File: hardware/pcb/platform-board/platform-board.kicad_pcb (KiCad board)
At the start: 2 copper layers, 55 x 65 mm, 9 parts, among them J1 Conn_01x09_Pin, J2 Conn_01x05_Pin, J3 Conn_01x05_Pin, J4 Conn_01x05_Pin, J5 Conn_01x05_Pin

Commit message: Initial boards for raw prototyping
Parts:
- J1: footprint Connector_PinHeader_2.54mm:PinHeader_1x09_P2.54mm_Horizontal -> TwinOak platform footprints:82155700
- moved J1 26.1 mm to (144.5, 91.7), turned to 0 degrees
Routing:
- net GND: track 71.1 -> 91.2 mm, vias 0 -> 1
- net Net-(J1-Pin_5): track 73.7 -> 53.8 mm, vias 2 -> 1
- net Net-(J1-Pin_6): track 73.7 -> 55.6 mm, vias 2 -> 1
- net Net-(J1-Pin_4): track 71.1 -> 53.8 mm, vias 2 -> 1
- net Net-(J1-Pin_7): track 71.1 -> 56.9 mm, vias 2 -> 1
- net Net-(J1-Pin_3): track 68.6 -> 55.0 mm, vias 2 -> 1
- net Net-(J1-Pin_8): track 68.6 -> 56.8 mm, vias 2 -> 1
- net Net-(J1-Pin_2): track 66.0 -> 54.4 mm, vias 2 -> 4
- net Net-(J1-Pin_9): track 66.0 -> 58.1 mm, vias 2 -> 1
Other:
- board text added: "Platform baseboard v1.0 TwinOak Standard Repeater"

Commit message: Platform rewire
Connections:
- J2 pad 2: Net-(J1-Pin_2) -> Net-(J1-Pin_3)
- J2 pad 3: Net-(J1-Pin_3) -> Net-(J1-Pin_5)
- J2 pad 4: Net-(J1-Pin_4) -> Net-(J1-Pin_7)
- J2 pad 5: Net-(J1-Pin_5) -> Net-(J1-Pin_9)
- J3 pad 2: Net-(J1-Pin_2) -> Net-(J1-Pin_3)
- J3 pad 3: Net-(J1-Pin_3) -> Net-(J1-Pin_5)
- J3 pad 4: Net-(J1-Pin_4) -> Net-(J1-Pin_7)
- J3 pad 5: Net-(J1-Pin_5) -> Net-(J1-Pin_9)
- J4 pad 2: Net-(J1-Pin_6) -> Net-(J1-Pin_2)
- J4 pad 3: Net-(J1-Pin_7) -> Net-(J1-Pin_4)
- J4 pad 4: Net-(J1-Pin_8) -> Net-(J1-Pin_6)
- J4 pad 5: Net-(J1-Pin_9) -> Net-(J1-Pin_8)
- J5 pad 2: Net-(J1-Pin_6) -> Net-(J1-Pin_2)
- J5 pad 3: Net-(J1-Pin_7) -> Net-(J1-Pin_4)
- J5 pad 4: Net-(J1-Pin_8) -> Net-(J1-Pin_6)
- J5 pad 5: Net-(J1-Pin_9) -> Net-(J1-Pin_8)
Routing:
- net Net-(J1-Pin_2): track 54.4 -> 62.0 mm, vias 4 -> 1
- net Net-(J1-Pin_4): track 53.8 -> 61.0 mm
- net Net-(J1-Pin_5): track 53.8 -> 58.9 mm
- net Net-(J1-Pin_6): track 55.6 -> 59.9 mm
- net Net-(J1-Pin_3): track 55.0 -> 58.8 mm, vias 1 -> 2
- net Net-(J1-Pin_7): track 56.9 -> 59.9 mm
- net Net-(J1-Pin_9): track 58.1 -> 61.0 mm
- net Net-(J1-Pin_8): track 56.8 -> 58.9 mm
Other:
- board text added: "Platform baseboard v1.1 TwinOak Standard Repeater"
- board text removed: "Platform baseboard v1.0 TwinOak Standard Repeater"

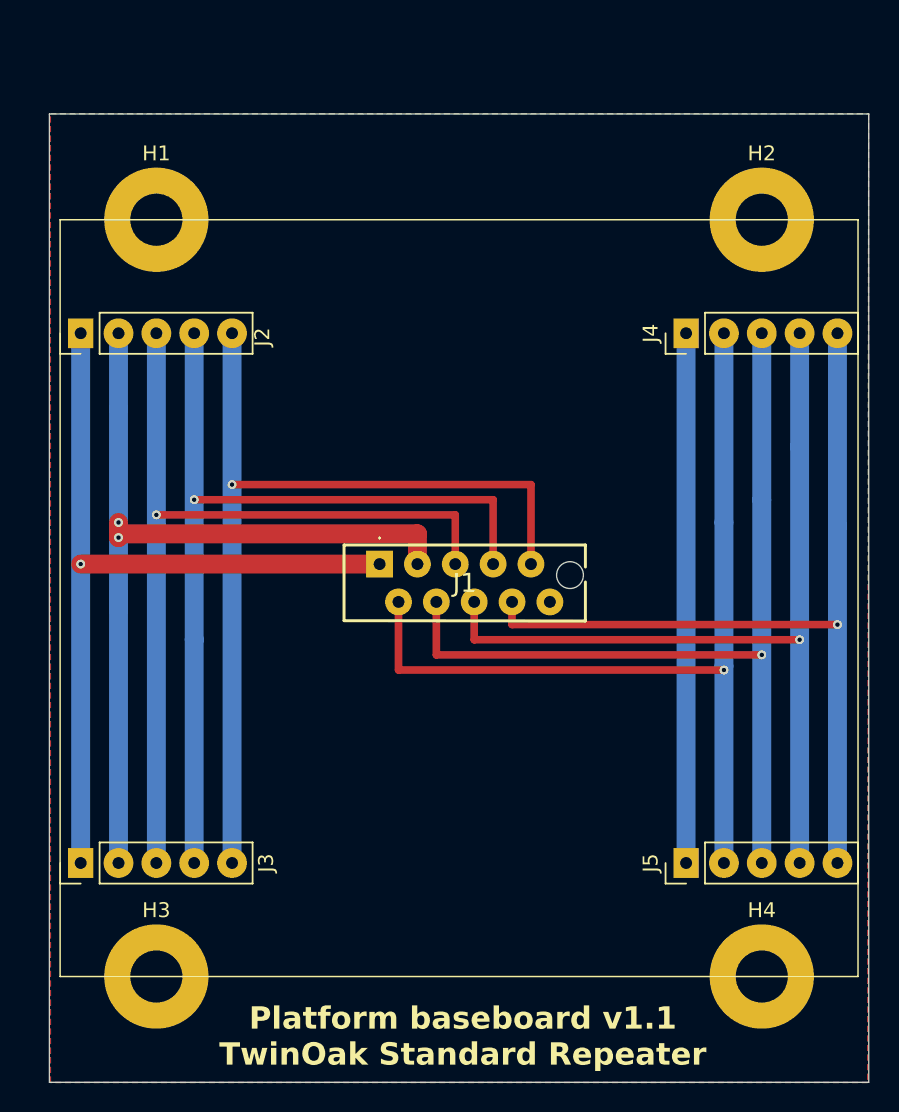
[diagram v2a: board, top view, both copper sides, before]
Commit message: Final PCB adjuments to rev 1.1
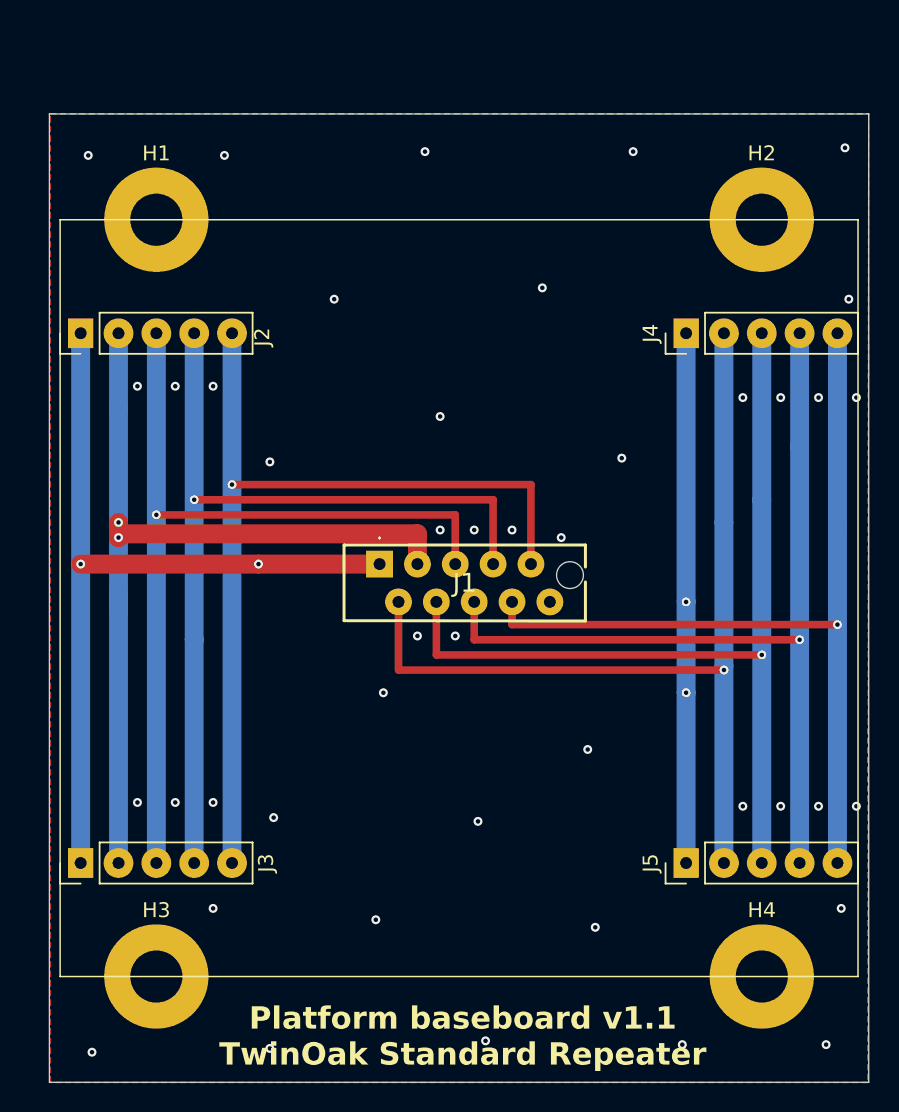
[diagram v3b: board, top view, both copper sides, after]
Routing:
- net GND: vias 1 -> 48
